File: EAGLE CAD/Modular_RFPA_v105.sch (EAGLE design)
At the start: 197 parts, among them IC201 74AHC1G14DBV, IC202 LM324D, J1 FUSE_2P, J2 KK_PCFAN, Q1 IRF540, Q101 IRF540, Q102 IRF540, Q2 IRF540, Q201 BSS123, T1 HP4_TRAFO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

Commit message: Work on IRF630 PA
Also add FET_parameters_sheet.csv
add IRF520 and IRF520N datasheets
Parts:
- C102, C104: value 0.1uF -> 22nF
- C105: value 0.1uF -> 12nF
- C106, C107, C109, C110, C17, C24, C25, C26, C27: value 0.1uF -> DNP
- C111, C112: value 22nF -> 2.2nF
- C113, C114: value 0.1uF -> 10nF
- C29: value 0.1uF -> SHORT
- L101, L102: value 1uH -> 150nH
- L6: value DR127 -> 22uH
- Q101: value IRF540 -> IRF630
- Q102: value IRF540 -> IRF520N
- R101, R105: value 1K -> 75
- R102, R106: value 1K -> 150
- R103: value 1K -> 4.99
- R104: value 1K -> 10
- R107, R109: value 1.0K -> 100
- R108, R110: value 1K -> 100
- R111, R112, R115, R116: value 1.0K -> DNP
- R113, R114: value 1.0K -> 15
- R117: value 1K -> 330
- R118, R120: value 1K -> 270
- R119: value 1K -> 2.74K
- R121, R123, R34: value 1K -> 2.7
- R122, R124: value 1K -> 6.8
- R30: value 1.0K -> 0
- R32, R33: value 1K -> 8.2
- R35: value 1K -> 3.3
- R40: value 0.33 -> 1.0
- R43: value 0.33 -> 0.5
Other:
- note added: "Circuit: * C:\Workspace\Git\BASIC_MRI_RFPA\LTSPICE simulations\RFPA_IRF630_pushpullx2_tran_param.asc Direct Newton iteration for .op point succeeded. pep: 50=(33.9794dB,0°) vd: 48=(33.6248dB,0°) vdmin: 12=(21.5836dB,0°) rload_lv_se_target: 12.96=(22.2521dB,0°) rload_lv_se: 12.96=(22.2521dB,0°) idmin: 0.5=(-6.0206dB,0°) id: 3.27777777777778=(10.3116dB,0°) gm0: 3.54=(10.9801dB,0°) gm: 1=(0dB,0°) rs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"
- note added: "Values shown in this branch are for preamp uses one pair of IRF520N"
- note added: "for preamp stage using one pair of IRF520N pep: 10=(20dB,0°) vd: 48=(33.6248dB,0°) vdmin: 26=(28.2995dB,0°) rload_lv_se_target: 24.2=(27.6763dB,0°) rload_lv_se: 24.2=(27.6763dB,0°) idmin: 0.5=(-6.0206dB,0°) id: 1.40909090909091=(2.97878dB,0°) gm0: 5.7=(15.1175dB,0°) gm: 0.5=(-6.0206dB,0°) rs: 1.82456140350877=(5.22317dB,0°) rgbias: 100=(40dB,0°) rsource_lv_se: 25=(27.9588dB,0°) rfb: 246.2=(47.825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"

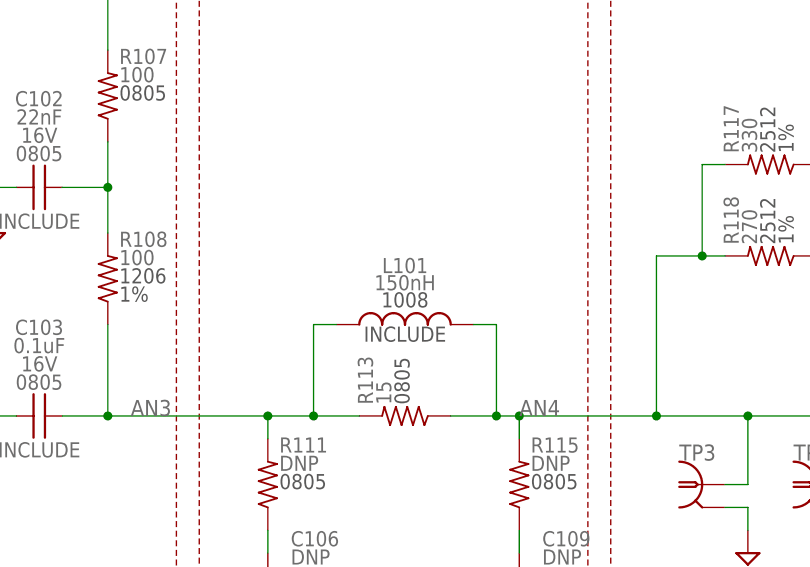
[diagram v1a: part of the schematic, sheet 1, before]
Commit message: Change Ldamp from 150nH to 47nH
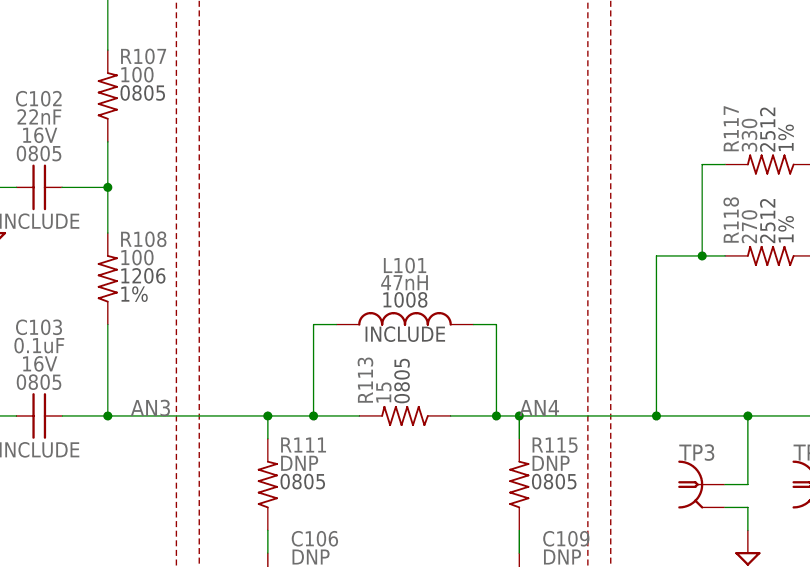
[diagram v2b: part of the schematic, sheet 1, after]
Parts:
- L101: value 150nH -> 47nH
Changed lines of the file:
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@@
 <part name="R121" library="MDT_R" deviceset="R" device="R2512" technology="R-1K-1%-2512-1W" value="2.7"/>
 <part name="R108" library="MDT_R" deviceset="R" device="R1206" technology="R-1.0K-1%-1206-0.25W" value="100"/>
-<part name="L101" library="MDT_L" deviceset="L_CHIP" device="1008" technology="L-1.0U-AIR-5%-1008-0.37A" value="150nH"/>
+<part name="L101" library="MDT_L" deviceset="L_CHIP" device="1008" technology="L-1.0U-AIR-5%-1008-0.37A" value="47nH"/>
 <part name="R105" library="MDT_R" deviceset="R" device="R1206" technology="R-1.0K-1%-1206-0.25W" value="75"/>
 <part name="R103" library="MDT_R" deviceset="R" device="R1206" technology="R-1.0K-1%-1206-0.25W" value="4.99"/>

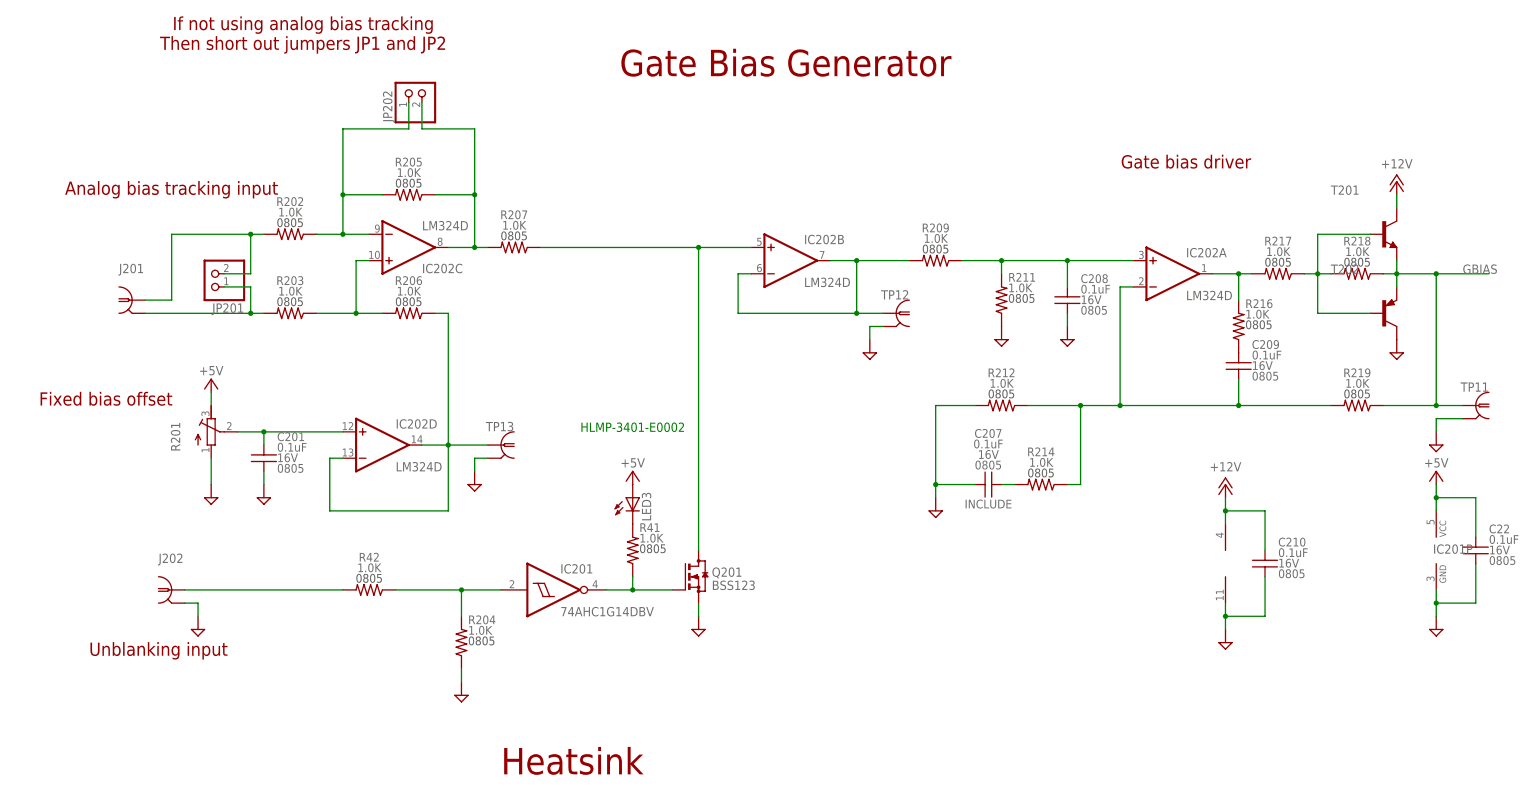
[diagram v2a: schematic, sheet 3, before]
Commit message: Update component values for gate bias driver
Change C209 from 220pF to 330pF
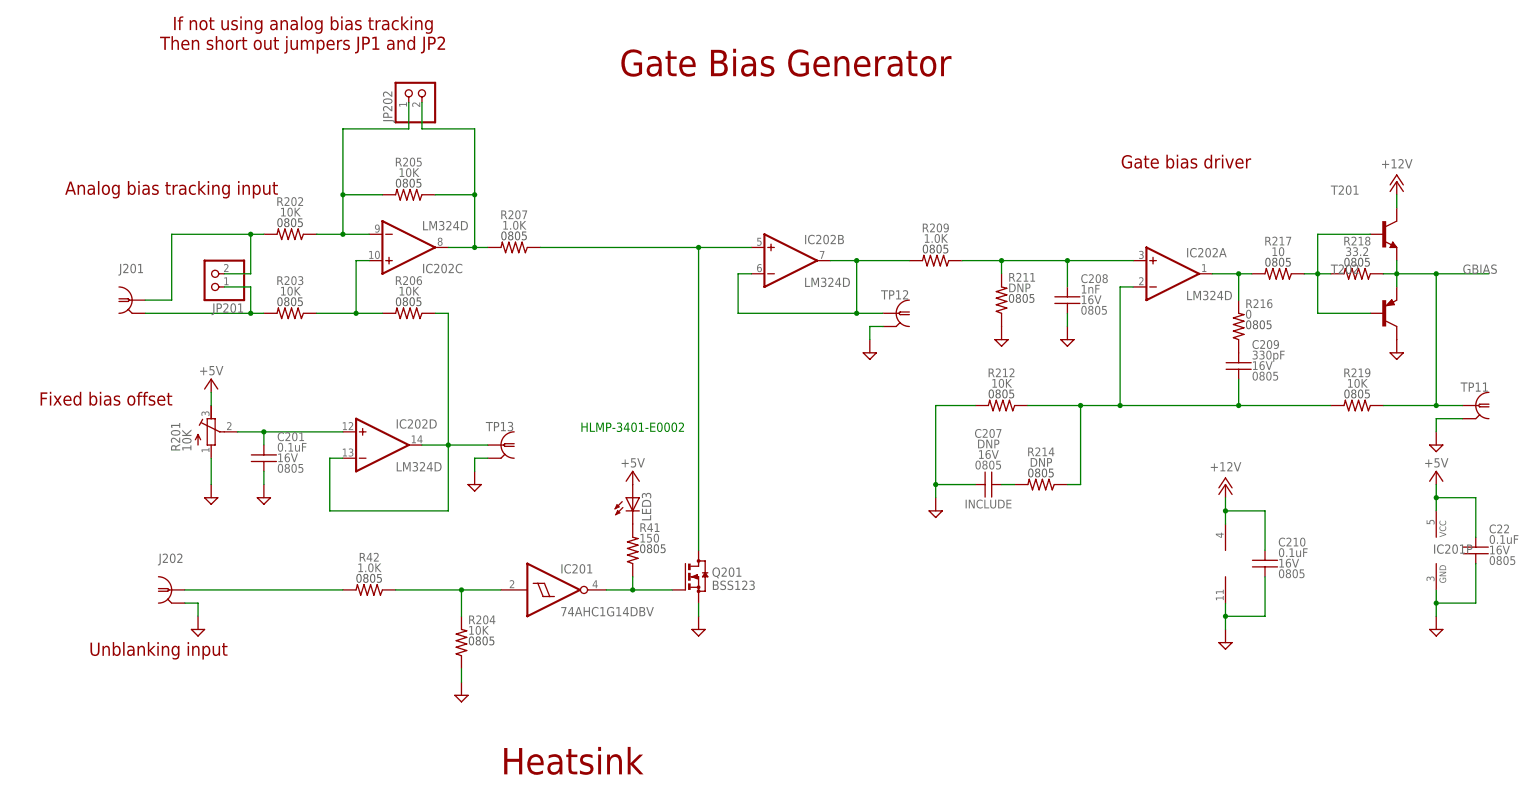
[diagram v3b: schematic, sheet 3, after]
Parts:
- C103: value 0.1uF -> 27nF
- C207: value 0.1uF -> DNP
- C208: value 0.1uF -> 1nF
- C209: value 0.1uF -> 330pF
- C28: value 0.1uF -> 47nF
- C29: value SHORT -> 100nF
- R201: value (none) -> 10K
- R202, R203, R204, R205, R206, R212, R219: value 1.0K -> 10K
- R211, R214: value 1.0K -> DNP
- R216: value 1.0K -> 0
- R217: value 1.0K -> 10
- R218: value 1.0K -> 33.2
- R41: value 1.0K -> 150
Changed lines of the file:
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@@
 <part name="SUPPLY207" library="supply2" deviceset="GND" device=""/>
 <part name="SUPPLY208" library="supply2" deviceset="GND" device=""/>
-<part name="R201" library="rcl" deviceset="R-TRIMM" device="3299W"/>
+<part name="R201" library="rcl" deviceset="R-TRIMM" device="3299W" value="10K"/>
 <part name="SUPPLY202" library="supply2" deviceset="GND" device=""/>
 <part name="SUPPLY204" library="supply2" deviceset="GND" device=""/>
@@
 <part name="C109" library="MDT_C" deviceset="C" device="0805_IPC" technology="C-0.1U-16V-0805-X7R" value="DNP"/>
 <part name="C106" library="MDT_C" deviceset="C" device="0805_IPC" technology="C-0.1U-16V-0805-X7R" value="DNP"/>
-<part name="C103" library="MDT_C" deviceset="C" device="0805_IPC" technology="C-0.1U-16V-0805-X7R" value="0.1uF">
+<part name="C103" library="MDT_C" deviceset="C" device="0805_IPC" technology="C-0.1U-16V-0805-X7R" value="27nF">
 <attribute name="BOM" value="INCLUDE"/>
 </part>
@@
 <part name="R102" library="MDT_R" deviceset="R" device="R1206" technology="R-1.0K-1%-1206-0.25W" value="150"/>
 <part name="R209" library="MDT_R" deviceset="R" device="0805_IPC" technology="R-1.0K-0.1%-0805-0.1W" value="1.0K"/>
-<part name="R217" library="MDT_R" deviceset="R" device="0805_IPC" technology="R-1.0K-0.1%-0805-0.1W" value="1.0K"/>
-<part name="R218" library="MDT_R" deviceset="R" device="0805_IPC" technology="R-1.0K-0.1%-0805-0.1W" value="1.0K"/>
-<part name="R219" library="MDT_R" deviceset="R" device="0805_IPC" technology="R-1.0K-0.1%-0805-0.1W" value="1.0K"/>
-<part name="R212" library="MDT_R" deviceset="R" device="0805_IPC" technology="R-1.0K-0.1%-0805-0.1W" value="1.0K"/>
-<part name="R214" library="MDT_R" deviceset="R" device="0805_IPC" technology="R-1.0K-0.1%-0805-0.1W" value="1.0K"/>
+<part name="R217" library="MDT_R" deviceset="R" device="0805_IPC" technology="R-1.0K-0.1%-0805-0.1W" value="10"/>
+<part name="R218" library="MDT_R" deviceset="R" device="0805_IPC" technology="R-1.0K-0.1%-0805-0.1W" value="33.2"/>
+<part name="R219" library="MDT_R" deviceset="R" device="0805_IPC" technology="R-1.0K-0.1%-0805-0.1W" value="10K"/>
+<part name="R212" library="MDT_R" deviceset="R" device="0805_IPC" technology="R-1.0K-0.1%-0805-0.1W" value="10K"/>
+<part name="R214" library="MDT_R" deviceset="R" device="0805_IPC" technology="R-1.0K-0.1%-0805-0.1W" value="DNP"/>
 <part name="R207" library="MDT_R" deviceset="R" device="0805_IPC" technology="R-1.0K-0.1%-0805-0.1W" value="1.0K"/>
-<part name="R203" library="MDT_R" deviceset="R" device="0805_IPC" technology="R-1.0K-0.1%-0805-0.1W" value="1.0K"/>
-<part name="R202" library="MDT_R" deviceset="R" device="0805_IPC" technology="R-1.0K-0.1%-0805-0.1W" value="1.0K"/>
-<part name="R206" library="MDT_R" deviceset="R" device="0805_IPC" technology="R-1.0K-0.1%-0805-0.1W" value="1.0K"/>
-<part name="R205" library="MDT_R" deviceset="R" device="0805_IPC" technology="R-1.0K-0.1%-0805-0.1W" value="1.0K"/>
-<part name="C209" library="MDT_C" deviceset="C" device="0805_IPC" technology="C-0.1U-16V-0805-X7R" value="0.1uF"/>
-<part name="R216" library="MDT_R" deviceset="R" device="0805_IPC" technology="R-1.0K-0.1%-0805-0.1W" value="1.0K"/>
-<part name="C207" library="MDT_C" deviceset="C" device="0805_IPC" technology="C-0.1U-16V-0805-X7R" value="0.1uF">
-<attribute name="BOM" value="INCLUDE"/>
-</part>
-<part name="C208" library="MDT_C" deviceset="C" device="0805_IPC" technology="C-0.1U-16V-0805-X7R" value="0.1uF"/>
+<part name="R203" library="MDT_R" deviceset="R" device="0805_IPC" technology="R-1.0K-0.1%-0805-0.1W" value="10K"/>
+<part name="R202" library="MDT_R" deviceset="R" device="0805_IPC" technology="R-1.0K-0.1%-0805-0.1W" value="10K"/>
+<part name="R206" library="MDT_R" deviceset="R" device="0805_IPC" technology="R-1.0K-0.1%-0805-0.1W" value="10K"/>
+<part name="R205" library="MDT_R" deviceset="R" device="0805_IPC" technology="R-1.0K-0.1%-0805-0.1W" value="10K"/>
+<part name="C209" library="MDT_C" deviceset="C" device="0805_IPC" technology="C-0.1U-16V-0805-X7R" value="330pF"/>
+<part name="R216" library="MDT_R" deviceset="R" device="0805_IPC" technology="R-1.0K-0.1%-0805-0.1W" value="0"/>
+<part name="C207" library="MDT_C" deviceset="C" device="0805_IPC" technology="C-0.1U-16V-0805-X7R" value="DNP">
+<attribute name="BOM" value="INCLUDE"/>
+</part>
+<part name="C208" library="MDT_C" deviceset="C" device="0805_IPC" technology="C-0.1U-16V-0805-X7R" value="1nF"/>
 <part name="C201" library="MDT_C" deviceset="C" device="0805_IPC" technology="C-0.1U-16V-0805-X7R" value="0.1uF"/>
 <part name="C210" library="MDT_C" deviceset="C" device="0805_IPC" technology="C-0.1U-16V-0805-X7R" value="0.1uF"/>
@@
 </part>
 <part name="R26" library="MDT_R" deviceset="R" device="R1206" technology="R-1.0K-1%-1206-0.25W" value="1K"/>
-<part name="R211" library="MDT_R" deviceset="R" device="0805_IPC" technology="R-1.0K-0.1%-0805-0.1W" value="1.0K"/>
-<part name="R204" library="MDT_R" deviceset="R" device="0805_IPC" technology="R-1.0K-0.1%-0805-0.1W" value="1.0K"/>
+<part name="R211" library="MDT_R" deviceset="R" device="0805_IPC" technology="R-1.0K-0.1%-0805-0.1W" value="DNP"/>
+<part name="R204" library="MDT_R" deviceset="R" device="0805_IPC" technology="R-1.0K-0.1%-0805-0.1W" value="10K"/>
 <part name="X1" library="con-wago-500" deviceset="W237-102" device=""/>
 <part name="SUPPLY17" library="supply2" deviceset="GND" device=""/>
@@
 <part name="LED3" library="led" deviceset="LED" device="5MM"/>
 <part name="P+7" library="supply1" deviceset="+5V" device=""/>
-<part name="R41" library="MDT_R" deviceset="R" device="0805_IPC" technology="R-1.0K-0.1%-0805-0.1W" value="1.0K"/>
+<part name="R41" library="MDT_R" deviceset="R" device="0805_IPC" technology="R-1.0K-0.1%-0805-0.1W" value="150"/>
 <part name="C25" library="MDT_C" deviceset="C" device="0805_IPC" technology="C-0.1U-16V-0805-X7R" value="DNP">
 <attribute name="BOM" value="INCLUDE"/>
@@
 <attribute name="BOM" value="INCLUDE"/>
 </part>
-<part name="C28" library="MDT_C" deviceset="C" device="0805_IPC" technology="C-0.1U-16V-0805-X7R" value="0.1uF">
+<part name="C28" library="MDT_C" deviceset="C" device="0805_IPC" technology="C-0.1U-16V-0805-X7R" value="47nF">
 <attribute name="BOM" value="INCLUDE"/>
 </part>
 <part name="C26" library="MDT_C" deviceset="C" device="C1812" value="DNP"/>
 <part name="C27" library="MDT_C" deviceset="C" device="C1812" value="DNP"/>
-<part name="C29" library="MDT_C" deviceset="C" device="C1812" value="SHORT"/>
+<part name="C29" library="MDT_C" deviceset="C" device="C1812" value="100nF"/>
 <part name="R42" library="MDT_R" deviceset="R" device="0805_IPC" technology="R-1.0K-0.1%-0805-0.1W" value="1.0K"/>
 <part name="R43" library="MDT_R" deviceset="R" device="R1206" technology="R-1.0K-1%-1206-0.25W" value="0.5"/>

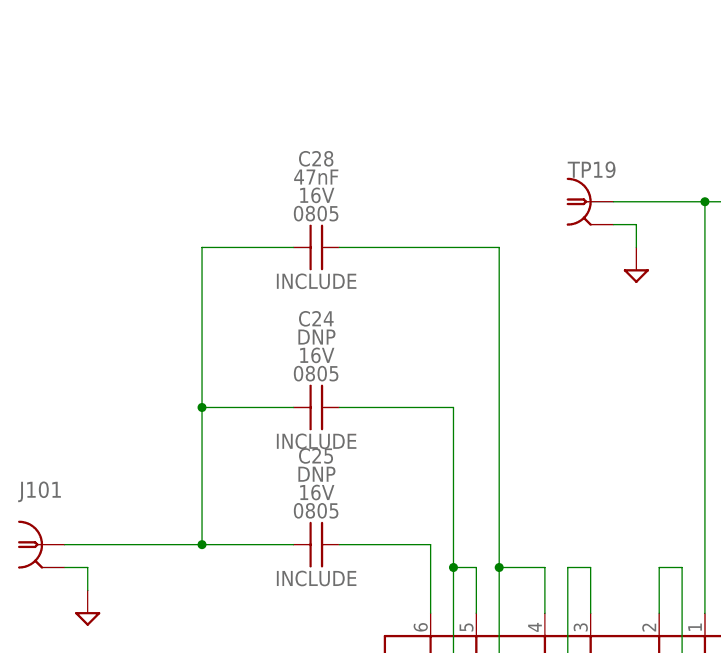
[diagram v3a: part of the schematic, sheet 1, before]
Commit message: Done testing for today
Seem to be getting significant loss across baluns
Measured input balun leakage at ~650nH (primary referred, both secondaries shorted to gnd)
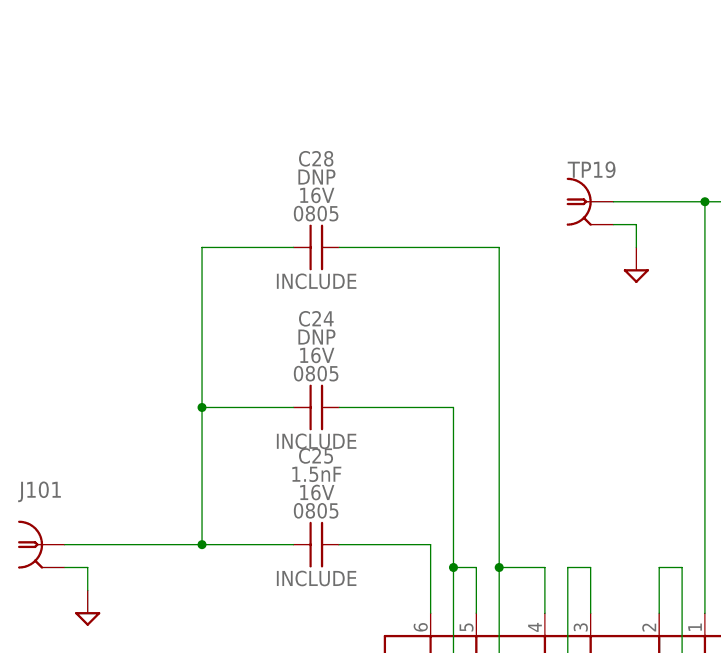
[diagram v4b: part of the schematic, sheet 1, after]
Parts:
- C25: value DNP -> 1.5nF
- C28: value 47nF -> DNP
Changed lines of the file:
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@@
 <part name="P+7" library="supply1" deviceset="+5V" device=""/>
 <part name="R41" library="MDT_R" deviceset="R" device="0805_IPC" technology="R-1.0K-0.1%-0805-0.1W" value="150"/>
-<part name="C25" library="MDT_C" deviceset="C" device="0805_IPC" technology="C-0.1U-16V-0805-X7R" value="DNP">
+<part name="C25" library="MDT_C" deviceset="C" device="0805_IPC" technology="C-0.1U-16V-0805-X7R" value="1.5nF">
 <attribute name="BOM" value="INCLUDE"/>
 </part>
@@
 <attribute name="BOM" value="INCLUDE"/>
 </part>
-<part name="C28" library="MDT_C" deviceset="C" device="0805_IPC" technology="C-0.1U-16V-0805-X7R" value="47nF">
+<part name="C28" library="MDT_C" deviceset="C" device="0805_IPC" technology="C-0.1U-16V-0805-X7R" value="DNP">
 <attribute name="BOM" value="INCLUDE"/>
 </part>
